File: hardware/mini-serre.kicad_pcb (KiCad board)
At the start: 2 copper layers, 115.6 x 53.3 mm, 35 parts, among them J0 POWER, J1 SERIAL, J2 ACT, J3 SEN, J4 I2C, J5 EXT, Q1 IMH20TR1G, Q2 VNN3NV04PTR, Q3 VNN3NV04PTR, Q4 VNN3NV04PTR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

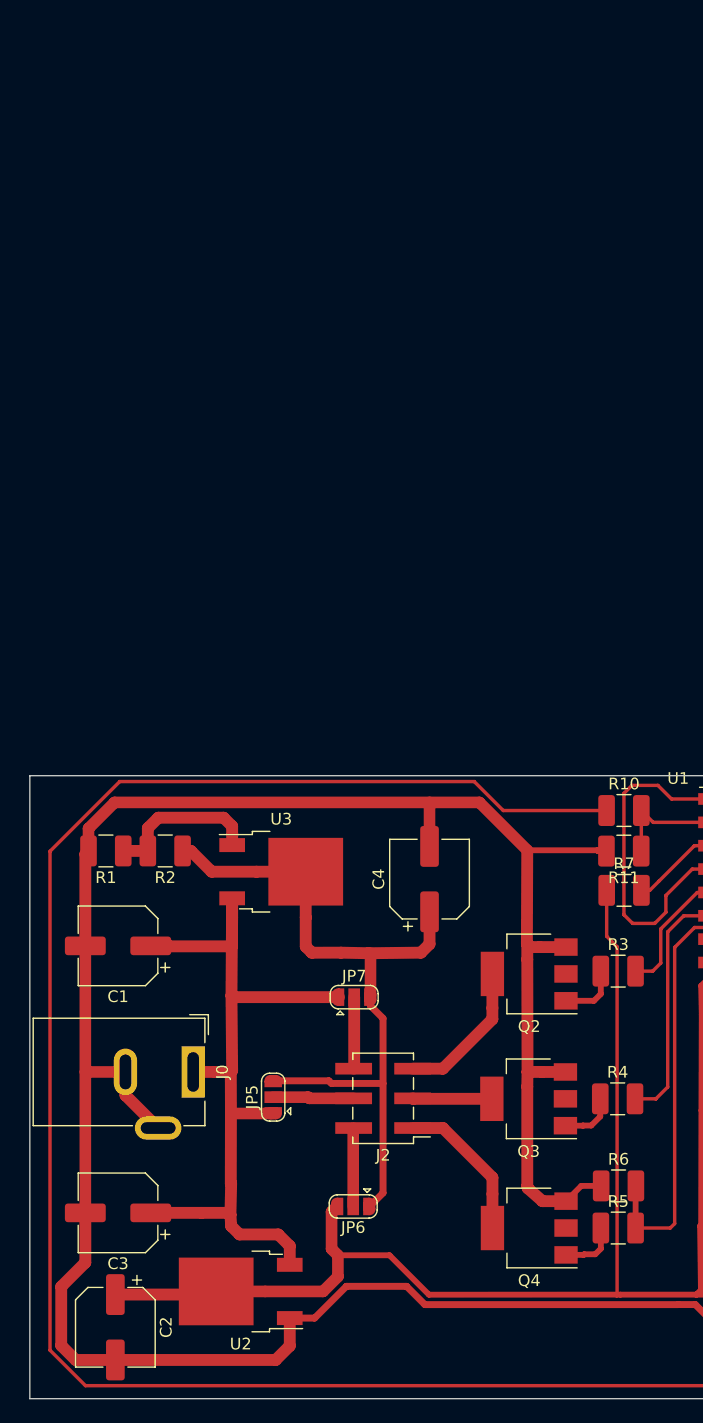
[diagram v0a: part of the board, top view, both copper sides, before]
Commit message: update schematics with buck converter, add part info and begin routing
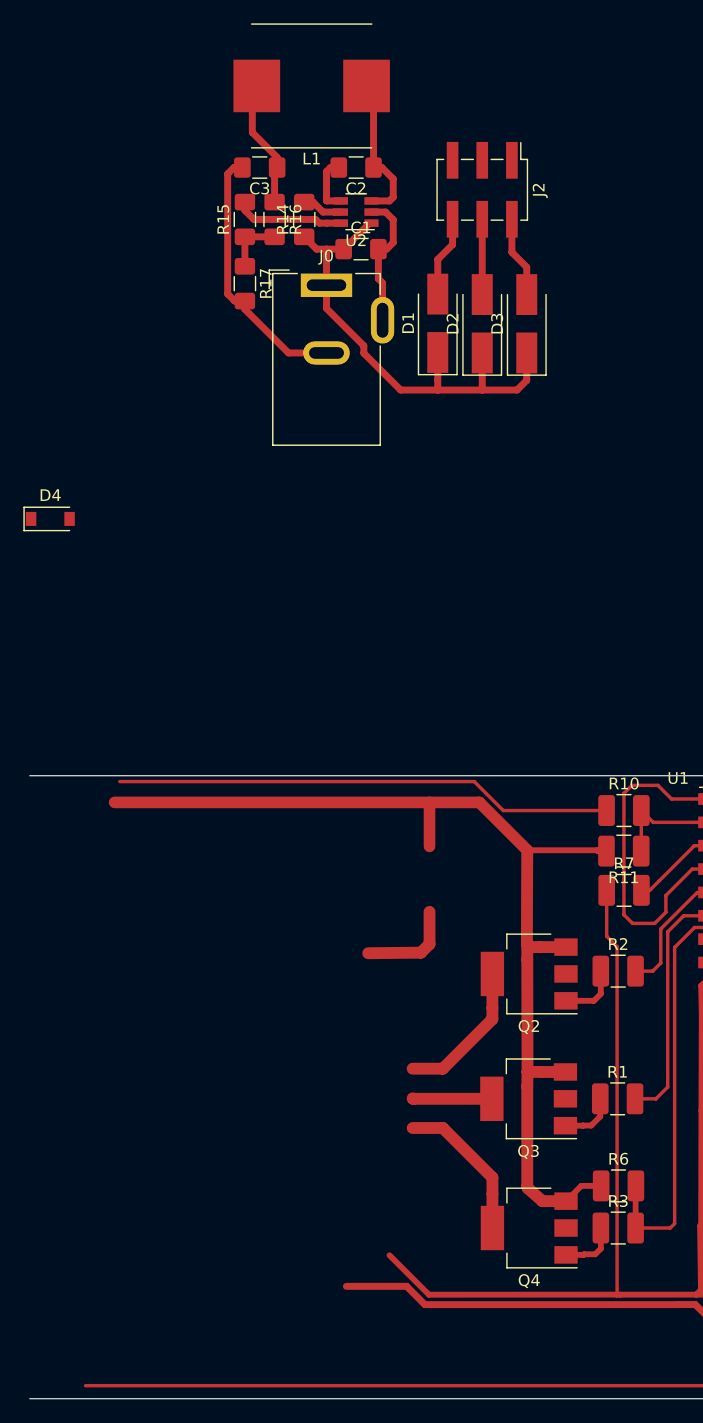
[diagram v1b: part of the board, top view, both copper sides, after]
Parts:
- removed C4: 10uF, Capacitor_SMD:CP_Elec_6.3x5.3
- removed JP5, JP7: 12V_OR_6V, mini-serre:SolderJumper-3_P1.3mm_Open_RoundedPad1.0x1.5mm
- removed JP6: 3V_OR_6V, mini-serre:SolderJumper-3_P1.3mm_Open_RoundedPad1.0x1.5mm
- removed the R1 at (20.5, 23.0)
- removed the R2 at (25.6, 23.0)
- removed U3: NCP1117-ADJ_TO252, Package_TO_SOT_SMD:TO-252-2
- added D1: D_Zener, Diode_SMD:D_SMA_Handsoldering, F.Cu at (48.9, -22.2)
- added D2: D_Zener, Diode_SMD:D_SMA_Handsoldering, F.Cu at (52.7, -22.2)
- added D3: D_Zener, Diode_SMD:D_SMA_Handsoldering, F.Cu at (56.5, -22.2)
- added D4: D_SHOTTKY, Diode_SMD:D_SOD-123, F.Cu at (15.7, -5.47)
- added L1: 6.5uH, Inductor_SMD:L_Taiyo-Yuden_NR-10050_9.8x10.0mm_HandSoldering, F.Cu at (38.1, -42.5)
- added R14: 100k, Resistor_SMD:R_1206_3216Metric_Pad1.42x1.75mm_HandSolder, F.Cu at (37.5, -31.1)
- added R15: 59k, Resistor_SMD:R_1206_3216Metric_Pad1.42x1.75mm_HandSolder, F.Cu at (32.4, -31.1)
- added R16: 40.2k, Resistor_SMD:R_1206_3216Metric_Pad1.42x1.75mm_HandSolder, F.Cu at (34.9, -31.1)
- added R17: 13k, Resistor_SMD:R_1206_3216Metric_Pad1.42x1.75mm_HandSolder, F.Cu at (32.4, -25.6)
- C1, C3: value 10uF -> 22uF; footprint Capacitor_SMD:CP_Elec_6.3x5.3 -> Capacitor_SMD:C_1206_3216Metric_Pad1.42x1.75mm_HandSolder
- C2: value 10uF -> 1uF; footprint Capacitor_SMD:CP_Elec_6.3x5.3 -> Capacitor_SMD:C_1206_3216Metric_Pad1.42x1.75mm_HandSolder
- U2: value NCP1117-3.3_TO252 -> AP65111AWU; footprint Package_TO_SOT_SMD:TO-252-2 -> Package_TO_SOT_SMD:TSOT-23-6
- moved C2 101.4 mm to (41.9, -35.6), turned to 180 degrees
- moved U2 92.9 mm to (41.9, -31.8)
- moved C3 90.3 mm to (33.7, -35.6)
- moved J2 78.3 mm to (52.7, -33.7), turned to 270 degrees
- moved J0 68.3 mm to (39.4, -25.5), turned to 0 degrees
- moved C1 63.2 mm to (42.3, -28.6), turned to 0 degrees
- renumbered R4 to R1, R3 to R2, R5 to R3
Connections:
- C2 pad 1: 3V3 -> Net-(C2-Pad1)
- C2 pad 2: GNDPWR -> Net-(C2-Pad2)
- C3 pad 1: 12V -> 3V3
- R9 pad 1: GNDPWR -> Net-(R9-Pad1)
- U2 pad 1: GNDPWR -> 12V
- U2 pad 2: 3V3 -> GNDPWR
- U2 pad 3: 12V -> Net-(C2-Pad1)
- U4 pad 15: (no net) -> Net-(R9-Pad1)
- U4 pad 2: SEL -> Net-(D4-Pad1)
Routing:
- net Net-(R10-Pad1): track 245.4 -> 189.9 mm
- net 6V: track 63.7 -> 8.32 mm
- net GNDPWR: track 380.1 -> 327.9 mm
- net 12V: track 69.6 -> 41.7 mm
- net 3V3: track 311.3 -> 291.8 mm
- net Net-(R1-Pad1): track 13.6 -> 0.00 mm
- net Net-(C2-Pad1): track 0.00 -> 12.9 mm
- net Net-(R15-Pad2): track 0.00 -> 9.38 mm
- net Net-(R15-Pad1): track 0.00 -> 5.06 mm
- net Net-(C2-Pad2): track 0.00 -> 4.93 mm
- net Net-(R14-Pad2): track 0.00 -> 3.49 mm
- net Net-(D1-Pad2): track 6.15 -> 6.93 mm

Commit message: backup before ground and power plane attempt
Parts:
- moved D4 118.1 mm to (125.1, 39.0), turned to 180 degrees
- moved L1 99.3 mm to (38.7, 56.8), turned to 0 degrees
- moved C3 85.9 mm to (43.2, 49.8), turned to 0 degrees
- moved C2 85.6 mm to (34.9, 49.8), turned to 0 degrees
- moved U2 78.0 mm to (34.9, 46.0), turned to 0 degrees
- moved R15 77.4 mm to (44.5, 45.3), turned to 270 degrees
- moved R16 76.8 mm to (41.9, 45.3), turned to 90 degrees
- moved R14 76.5 mm to (39.4, 45.3), turned to 270 degrees
- moved R17 72.4 mm to (46.9, 45.3)
- moved C1 71.8 mm to (34.5, 42.8), turned to 180 degrees
- moved J0 60.8 mm to (43.2, 35.2), turned to 270 degrees
- moved J2 57.7 mm to (47.0, 23.7), turned to 180 degrees
- moved D3 54.0 mm to (35.5, 27.6), turned to 0 degrees
- moved D2 49.0 mm to (35.5, 23.7), turned to 0 degrees
- moved D1 44.2 mm to (35.6, 19.9), turned to 0 degrees
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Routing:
- net Net-(R10-Pad1): track 189.9 -> 51.7 mm, vias 0 -> 2
- net 3V3: track 291.8 -> 363.1 mm
- net SEL: track 36.5 -> 72.5 mm
- net SCL: track 43.2 -> 19.3 mm
- net RESET: track 102.1 -> 81.7 mm
- net D2: track 6.80 -> 27.1 mm
- net Net-(J1-Pad1): track 33.7 -> 13.5 mm
- net IO0: track 36.4 -> 16.9 mm
- net Net-(J1-Pad2): track 38.4 -> 19.4 mm
- net D3: track 12.9 -> 31.7 mm
- net GNDPWR: track 327.9 -> 314.5 mm
- net SDA: track 38.2 -> 27.0 mm
- net 6V: track 8.32 -> 0.00 mm
- net D1: track 12.5 -> 19.0 mm
- net Net-(R9-Pad1): track 0.00 -> 6.49 mm
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
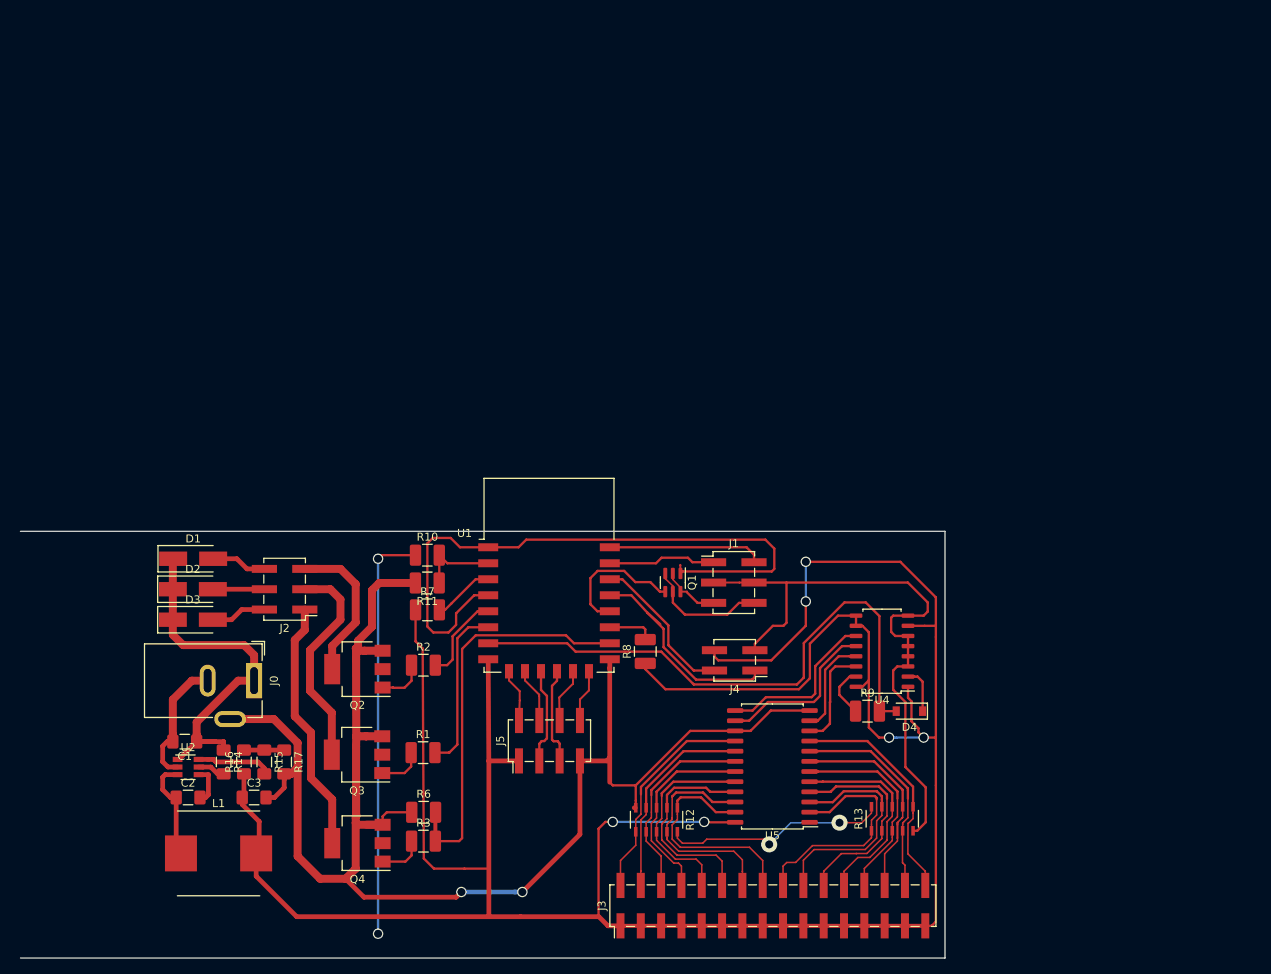
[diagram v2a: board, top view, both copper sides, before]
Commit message: splitted in 3 modules : power in, power outputs, analog multiplexer, logic
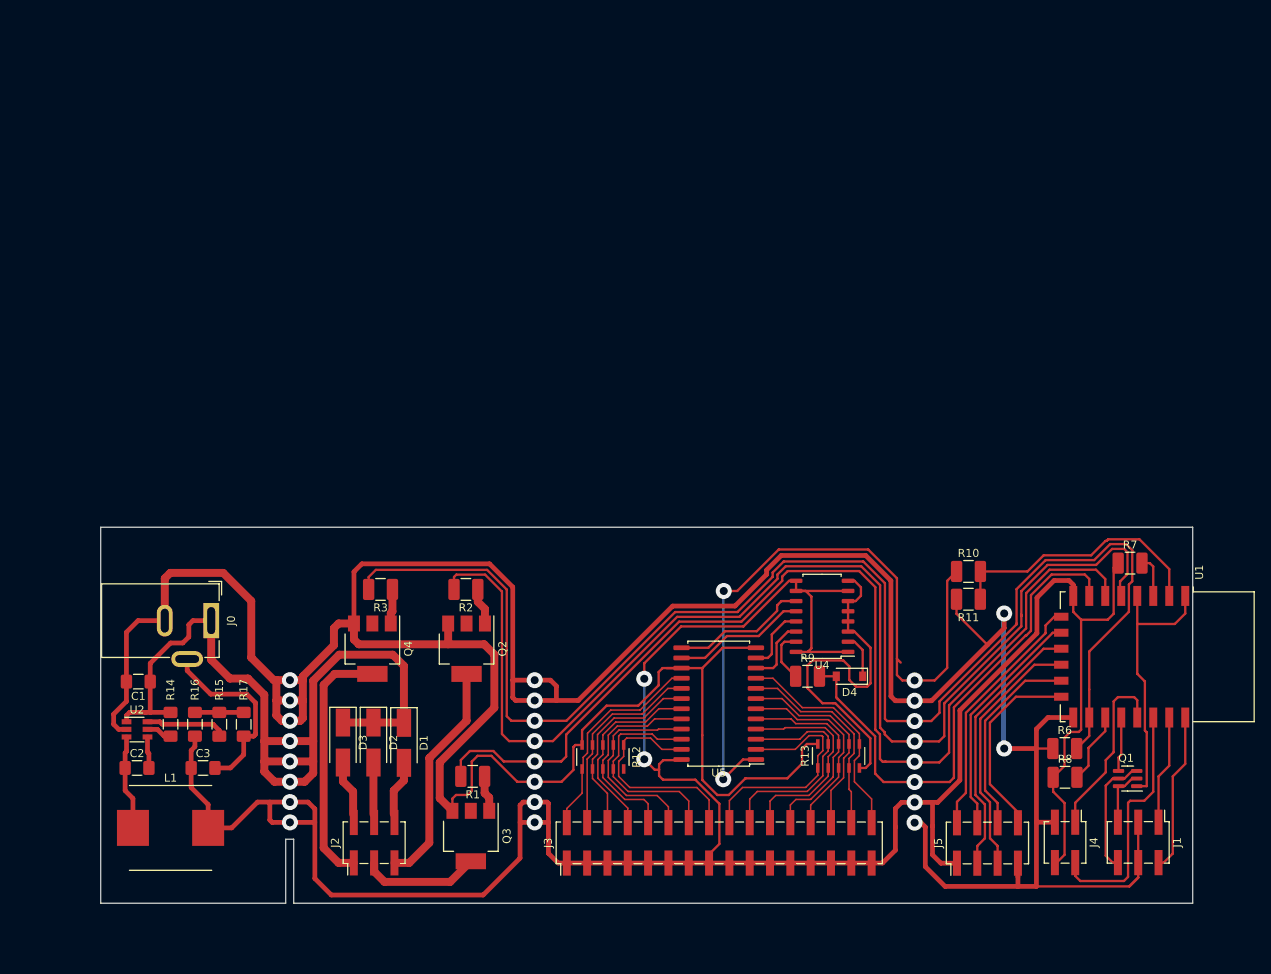
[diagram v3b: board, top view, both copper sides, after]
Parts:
- moved R7 88.0 mm to (152.7, 20.5)
- moved R6 80.5 mm to (144.5, 43.7)
- moved U1 76.7 mm to (156.1, 32.2), turned to 270 degrees
- moved R10 67.7 mm to (132.5, 21.5)
- moved R11 67.7 mm to (132.5, 25.0)
- moved Q1 61.9 mm to (152.4, 47.4), turned to 180 degrees
- moved J1 60.1 mm to (153.7, 55.4), turned to 270 degrees
- moved J5 56.2 mm to (134.8, 55.5)
- moved R8 54.8 mm to (144.5, 47.3), turned to 0 degrees
- moved J4 47.2 mm to (144.5, 55.4), turned to 270 degrees
- moved D1 35.0 mm to (61.9, 43.0), turned to 270 degrees
- moved J2 33.6 mm to (58.2, 55.4), turned to 90 degrees
- moved R3 31.9 mm to (59.0, 23.8), turned to 180 degrees
- moved D2 29.6 mm to (58.1, 42.9), turned to 270 degrees
- moved Q4 24.4 mm to (58.0, 31.2), turned to 270 degrees
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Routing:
- net GNDPWR: track 314.5 -> 528.7 mm, vias 4 -> 10
- net SIG2: track 11.1 -> 155.1 mm, vias 0 -> 2
- net IO15: track 50.3 -> 181.9 mm, vias 0 -> 2
- net SIG1: track 20.9 -> 136.2 mm, vias 0 -> 2
- net 12V: track 45.8 -> 105.5 mm, vias 0 -> 3
- net RESET: track 81.7 -> 34.3 mm
- net 3V3: track 363.1 -> 326.7 mm, vias 6 -> 7
- net Net-(R10-Pad1): track 51.7 -> 86.4 mm, vias 2 -> 3
- net Net-(J5-Pad2): track 6.71 -> 31.7 mm
- net MM: track 10.0 -> 33.6 mm
- net Net-(J5-Pad4): track 6.89 -> 29.4 mm
- net IO9: track 12.1 -> 33.4 mm
- net IO10: track 12.2 -> 31.9 mm
- net Net-(J5-Pad6): track 6.87 -> 25.0 mm
- net Net-(J5-Pad8): track 6.62 -> 24.4 mm
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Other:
- board size 115.6 x 53.3 mm -> 136.5 x 47 mm

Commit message: Current state
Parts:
- added G***: LOGO, mini-serre:mini-serre-logo, F.Cu at (84.5, 21.5)
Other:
- outline, holes or cut-outs redrawn
- board text added: "FabLab | La Chaux-de-Fonds Mini-Serre 0.1 / OSHW Input 4.5-18v, Output 4.5-18V / 3.3V"
